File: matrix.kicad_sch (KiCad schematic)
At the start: 129 parts

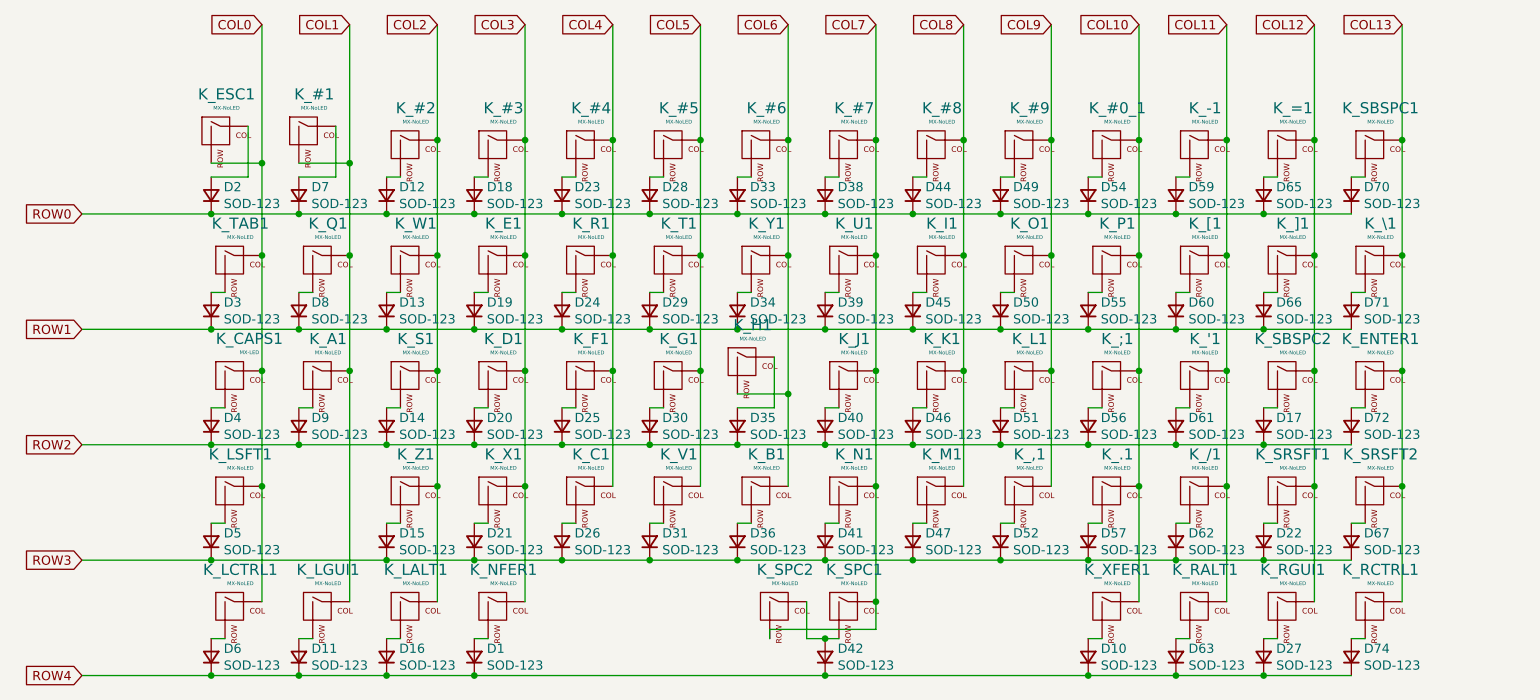
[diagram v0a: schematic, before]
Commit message: Edit Key Matrix
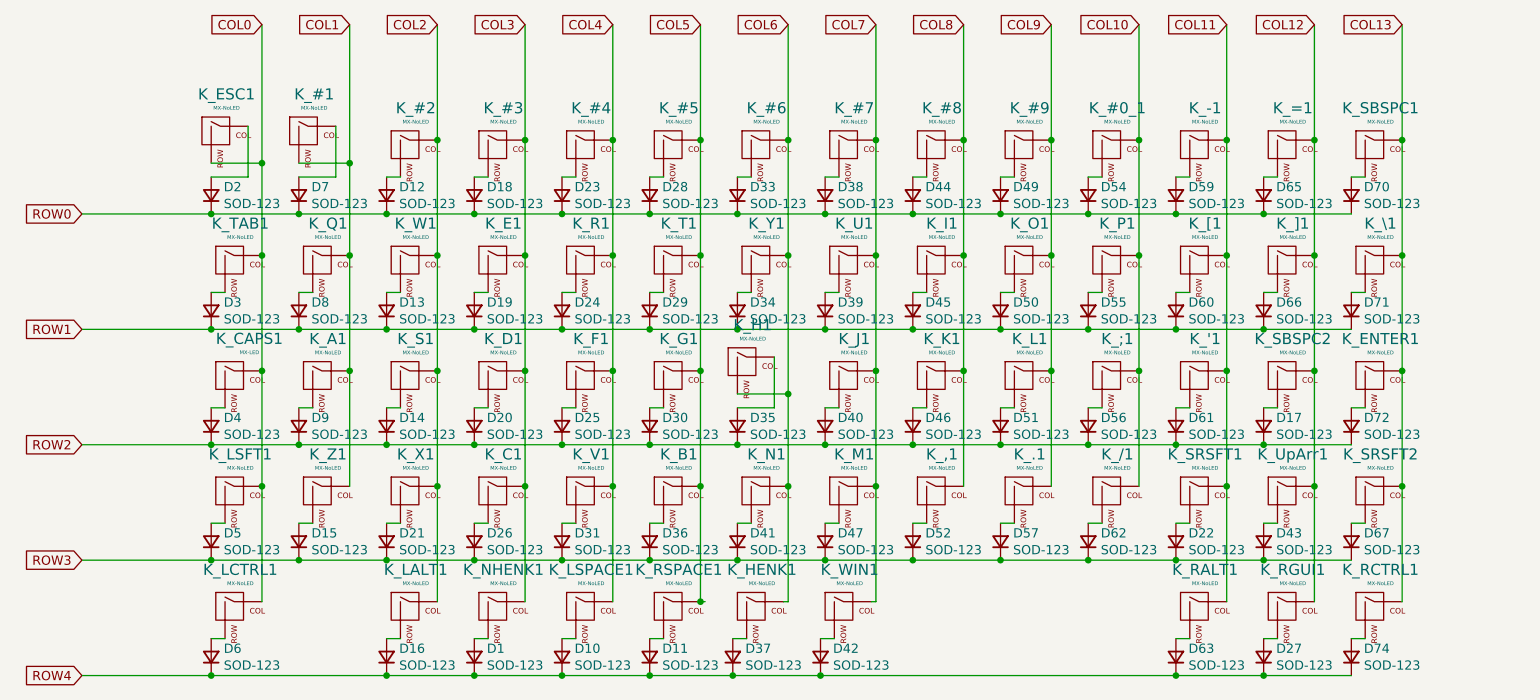
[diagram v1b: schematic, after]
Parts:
- removed K_LGUI1, K_SPC2: MX-NoLED, MX_Only:MXOnly-1U-Hotswap, symbol MX_Alps_Hybrid:MX-NoLED
- removed K_SPC1: MX-NoLED, MX_Only:MXOnly-6U-Centered-Hotswap-ReversedStabilizers, symbol MX_Alps_Hybrid:MX-NoLED
- removed K_XFER1: MX-NoLED, MX_Only:MXOnly-1.25U-Hotswap, symbol MX_Alps_Hybrid:MX-NoLED
- added D37, D43: SOD-123, Diode_SMD:D_SOD-123, symbol Device:D_Small
- added K_HENK1, K_UpArr1, K_WIN1: MX-NoLED, MX_Only:MXOnly-1U-Hotswap, symbol MX_Alps_Hybrid:MX-NoLED
- added K_LSPACE1, K_RSPACE1: MX-NoLED, MX_Only:MXOnly-1.25U-Hotswap, symbol MX_Alps_Hybrid:MX-NoLED
- renumbered K_NFER1 to K_NHENK1
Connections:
- net COL1: now also K_Z1.1 (COL)
- net COL10: now also K_/1.1 (COL); no longer K_.1.1 (COL)
- net COL11: now also K_SRSFT1.1 (COL); no longer K_/1.1 (COL)
- net COL12: now also K_UpArr1.1 (COL); no longer K_SRSFT1.1 (COL)
- net COL2: now also K_X1.1 (COL); no longer K_Z1.1 (COL)
- net COL3: now also K_C1.1 (COL); no longer K_X1.1 (COL)
- net COL4: now also K_V1.1 (COL), K_LSPACE1.1 (COL); no longer K_C1.1 (COL)
- net COL5: now also K_B1.1 (COL), K_RSPACE1.1 (COL); no longer K_V1.1 (COL)
- net COL6: now also K_N1.1 (COL), K_HENK1.1 (COL); no longer K_B1.1 (COL)
- net COL7: now also K_M1.1 (COL), K_WIN1.1 (COL); no longer K_N1.1 (COL)
- net COL8: now also K_,1.1 (COL); no longer K_M1.1 (COL)
- net COL9: now also K_.1.1 (COL); no longer K_,1.1 (COL)
- net ROW3: now also D43.1 (K)
- net ROW4: now also D37.1 (K)
- net at D42.2 (A): now also K_WIN1.2 (ROW)
- net at D11.2 (A): now also K_RSPACE1.2 (ROW)
- net at D10.2 (A): now also K_LSPACE1.2 (ROW)
- new net: D43.2 (A), K_UpArr1.2 (ROW)
- new net: D37.2 (A), K_HENK1.2 (ROW)
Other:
- moved on the sheet: D15, D21, D22, D26, D31, D36, D41, D47, D52, D57, D62, K_,1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

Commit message: edit footprint of Keyswitches.
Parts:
- K_LCTRL1, K_NHENK1: footprint MX_Only:MXOnly-1.25U-Hotswap -> MX_Only:MXOnly-1U-Hotswap
- K_LSFT1: footprint MX_Only:MXOnly-2.25U-Hotswap -> MX_Only:MXOnly-2U-Hotswap
- K_SRSFT2: footprint MX_Only:MXOnly-1.75U-Hotswap -> MX_Only:MXOnly-1U-Hotswap
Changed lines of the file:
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@@
       (effects (font (size 0.508 0.508)))
     )
-    (property "Footprint" "MX_Only:MXOnly-2.25U-Hotswap" (id 2) (at 60.325 102.235 0)
+    (property "Footprint" "MX_Only:MXOnly-2U-Hotswap" (id 2) (at 60.325 102.235 0)
       (effects (font (size 1.524 1.524)) hide)
     )
@@
       (effects (font (size 0.508 0.508)))
     )
-    (property "Footprint" "MX_Only:MXOnly-1.75U-Hotswap" (id 2) (at 217.17 102.235 0)
+    (property "Footprint" "MX_Only:MXOnly-1U-Hotswap" (id 2) (at 217.17 102.235 0)
       (effects (font (size 1.524 1.524)) hide)
     )
@@
       (effects (font (size 0.508 0.508)))
     )
-    (property "Footprint" "MX_Only:MXOnly-1.25U-Hotswap" (id 2) (at 60.325 118.11 0)
+    (property "Footprint" "MX_Only:MXOnly-1U-Hotswap" (id 2) (at 60.325 118.11 0)
       (effects (font (size 1.524 1.524)) hide)
     )
@@
       (effects (font (size 0.508 0.508)))
     )
-    (property "Footprint" "MX_Only:MXOnly-1.25U-Hotswap" (id 2) (at 96.52 118.11 0)
-      (effects (font (size 1.524 1.524)) hide)
-    )
+    (property "Footprint" "MX_Only:MXOnly-1U-Hotswap" (id 2) (at 96.52 118.11 0)
+      (effects (font (size 1.524 1.524)) hide)
+    )

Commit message: Modify Symbol Name
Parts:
- renumbered K_RGUI1 to K_DOWN1, K_RALT1 to K_LEFT1, K_\1 to K_PIPE1, K_RCTRL1 to K_RIGHT1, K_SRSFT2 to K_RSFT1, K_SRSFT1 to K_UNSC1, K_UpArr1 to K_UP1
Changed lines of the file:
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@@
   (symbol (lib_id "MX_Alps_Hybrid:MX-NoLED") (at 233.045 69.85 0) (unit 1)
     (in_bom yes) (on_board yes)
-    (property "Reference" "K_\\1" (id 0) (at 233.8832 64.1858 0)
+    (property "Reference" "K_PIPE1" (id 0) (at 233.8832 64.1858 0)
       (effects (font (size 1.524 1.524)))
     )
@@
   (symbol (lib_id "MX_Alps_Hybrid:MX-NoLED") (at 233.045 101.6 0) (unit 1)
     (in_bom yes) (on_board yes)
-    (property "Reference" "K_SRSFT2" (id 0) (at 233.8832 95.9358 0)
+    (property "Reference" "K_RSFT1" (id 0) (at 233.8832 95.9358 0)
       (effects (font (size 1.524 1.524)))
     )
@@
   (symbol (lib_id "MX_Alps_Hybrid:MX-NoLED") (at 208.915 117.475 0) (unit 1)
     (in_bom yes) (on_board yes)
-    (property "Reference" "K_RALT1" (id 0) (at 209.7532 111.8108 0)
+    (property "Reference" "K_LEFT1" (id 0) (at 209.7532 111.8108 0)
       (effects (font (size 1.524 1.524)))
     )
@@
   (symbol (lib_id "MX_Alps_Hybrid:MX-NoLED") (at 233.045 117.475 0) (unit 1)
     (in_bom yes) (on_board yes)
-    (property "Reference" "K_RCTRL1" (id 0) (at 233.8832 111.8108 0)
+    (property "Reference" "K_RIGHT1" (id 0) (at 233.8832 111.8108 0)
       (effects (font (size 1.524 1.524)))
     )
@@
   (symbol (lib_id "MX_Alps_Hybrid:MX-NoLED") (at 208.915 101.6 0) (unit 1)
     (in_bom yes) (on_board yes)
-    (property "Reference" "K_SRSFT1" (id 0) (at 209.7532 95.9358 0)
+    (property "Reference" "K_UNSC1" (id 0) (at 209.7532 95.9358 0)
       (effects (font (size 1.524 1.524)))
     )
@@
   (symbol (lib_id "MX_Alps_Hybrid:MX-NoLED") (at 220.98 117.475 0) (unit 1)
     (in_bom yes) (on_board yes)
-    (property "Reference" "K_RGUI1" (id 0) (at 221.8182 111.8108 0)
+    (property "Reference" "K_DOWN1" (id 0) (at 221.8182 111.8108 0)
       (effects (font (size 1.524 1.524)))
     )
@@
   (symbol (lib_id "MX_Alps_Hybrid:MX-NoLED") (at 220.98 101.6 0) (unit 1)
     (in_bom yes) (on_board yes)
-    (property "Reference" "K_UpArr1" (id 0) (at 221.8182 95.9358 0)
-      (effects (font (size 1.524 1.524)))
-    )
+    (property "Reference" "K_UP1" (id 0) (at 221.8182 95.9358 0)
+      (effects (font (size 1.524 1.524)))
+    )

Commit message: Diodeの配置完了
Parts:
- renumbered K_'1 to K_:1, K_[1 to K_@1, K_SBSPC2 to K_BKSPC1, K_SBSPC1 to K_PIPE1, K_]1 to K_[1, K_PIPE1 to K_]2
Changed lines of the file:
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@@
   (symbol (lib_id "MX_Alps_Hybrid:MX-NoLED") (at 233.045 53.975 0) (unit 1)
     (in_bom yes) (on_board yes)
-    (property "Reference" "K_SBSPC1" (id 0) (at 233.8832 48.3108 0)
+    (property "Reference" "K_PIPE1" (id 0) (at 233.8832 48.3108 0)
       (effects (font (size 1.524 1.524)))
     )
@@
   (symbol (lib_id "MX_Alps_Hybrid:MX-NoLED") (at 208.915 69.85 0) (unit 1)
     (in_bom yes) (on_board yes)
-    (property "Reference" "K_[1" (id 0) (at 209.7532 64.1858 0)
+    (property "Reference" "K_@1" (id 0) (at 209.7532 64.1858 0)
       (effects (font (size 1.524 1.524)))
     )
@@
   (symbol (lib_id "MX_Alps_Hybrid:MX-NoLED") (at 220.98 69.85 0) (unit 1)
     (in_bom yes) (on_board yes)
-    (property "Reference" "K_]1" (id 0) (at 221.8182 64.1858 0)
+    (property "Reference" "K_[1" (id 0) (at 221.8182 64.1858 0)
       (effects (font (size 1.524 1.524)))
     )
@@
   (symbol (lib_id "MX_Alps_Hybrid:MX-NoLED") (at 233.045 69.85 0) (unit 1)
     (in_bom yes) (on_board yes)
-    (property "Reference" "K_PIPE1" (id 0) (at 233.8832 64.1858 0)
+    (property "Reference" "K_]2" (id 0) (at 233.8832 64.1858 0)
       (effects (font (size 1.524 1.524)))
     )
@@
   (symbol (lib_id "MX_Alps_Hybrid:MX-NoLED") (at 208.915 85.725 0) (unit 1)
     (in_bom yes) (on_board yes)
-    (property "Reference" "K_'1" (id 0) (at 209.7532 80.0608 0)
+    (property "Reference" "K_:1" (id 0) (at 209.7532 80.0608 0)
       (effects (font (size 1.524 1.524)))
     )
@@
   (symbol (lib_id "MX_Alps_Hybrid:MX-NoLED") (at 220.98 85.725 0) (unit 1)
     (in_bom yes) (on_board yes)
-    (property "Reference" "K_SBSPC2" (id 0) (at 221.8182 80.0608 0)
-      (effects (font (size 1.524 1.524)))
-    )
+    (property "Reference" "K_BKSPC1" (id 0) (at 221.8182 80.0608 0)
+      (effects (font (size 1.524 1.524)))
+    )

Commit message: 時間的にいったんここまで
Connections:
- net COL6: now also K_H1.1 (COL); no longer K_H1.2 (ROW)
- net at D35.2 (A): now also K_H1.2 (ROW); no longer K_H1.1 (COL)
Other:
- moved on the sheet: K_H1
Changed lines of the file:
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@@
   (junction (at 181.61 110.49) (diameter 0) (color 0 0 0 0)
   )
+  (junction (at 152.4 84.455) (diameter 0) (color 0 0 0 0)
+  )
   (junction (at 109.22 78.74) (diameter 0) (color 0 0 0 0)
   )
@@
   (junction (at 73.025 62.865) (diameter 0) (color 0 0 0 0)
   )
-  (junction (at 152.4 87.63) (diameter 0) (color 0 0 0 0)
-  )
   (junction (at 188.595 52.705) (diameter 0) (color 0 0 0 0)
   )
@@
     (stroke (width 0) (type default) (color 0 0 0 0))
   )
-  (wire (pts (xy 145.415 89.535) (xy 150.495 89.535))
-    (stroke (width 0) (type default) (color 0 0 0 0))
-  )
   (wire (pts (xy 193.675 110.49) (xy 181.61 110.49))
     (stroke (width 0) (type default) (color 0 0 0 0))
@@
     (stroke (width 0) (type default) (color 0 0 0 0))
   )
-  (wire (pts (xy 145.415 87.63) (xy 152.4 87.63))
-    (stroke (width 0) (type default) (color 0 0 0 0))
-  )
   (wire (pts (xy 229.87 94.615) (xy 217.805 94.615))
     (stroke (width 0) (type default) (color 0 0 0 0))
@@
     (stroke (width 0) (type default) (color 0 0 0 0))
   )
+  (wire (pts (xy 145.415 89.535) (xy 147.32 89.535))
+    (stroke (width 0) (type default) (color 0 0 0 0))
+  )
   (wire (pts (xy 181.61 62.865) (xy 193.675 62.865))
     (stroke (width 0) (type default) (color 0 0 0 0))
@@
     (stroke (width 0) (type default) (color 0 0 0 0))
   )
+  (wire (pts (xy 152.4 84.455) (xy 152.4 100.33))
+    (stroke (width 0) (type default) (color 0 0 0 0))
+  )
   (wire (pts (xy 73.025 94.615) (xy 55.245 94.615))
     (stroke (width 0) (type default) (color 0 0 0 0))
@@
     (stroke (width 0) (type default) (color 0 0 0 0))
   )
-  (wire (pts (xy 152.4 68.58) (xy 152.4 87.63))
+  (wire (pts (xy 152.4 68.58) (xy 152.4 84.455))
     (stroke (width 0) (type default) (color 0 0 0 0))
   )
@@
     (stroke (width 0) (type default) (color 0 0 0 0))
   )
-  (wire (pts (xy 150.495 82.55) (xy 150.495 89.535))
-    (stroke (width 0) (type default) (color 0 0 0 0))
-  )
   (wire (pts (xy 73.025 121.285) (xy 74.93 121.285))
     (stroke (width 0) (type default) (color 0 0 0 0))
@@
   )
   (wire (pts (xy 85.09 62.865) (xy 97.155 62.865))
-    (stroke (width 0) (type default) (color 0 0 0 0))
-  )
-  (wire (pts (xy 152.4 87.63) (xy 152.4 100.33))
     (stroke (width 0) (type default) (color 0 0 0 0))
   )
@@
     (pin "2")
   )
-  (symbol (lib_id "MX_Alps_Hybrid:MX-NoLED") (at 146.685 83.82 0) (unit 1)
-    (in_bom yes) (on_board yes)
-    (property "Reference" "K_H1" (id 0) (at 147.5232 78.1558 0)
-      (effects (font (size 1.524 1.524)))
-    )
-    (property "Value" "MX-NoLED" (id 1) (at 147.5232 80.0354 0)
-      (effects (font (size 0.508 0.508)))
-    )
-    (property "Footprint" "MX_Only:MXOnly-1U-Hotswap" (id 2) (at 130.81 84.455 0)
-      (effects (font (size 1.524 1.524)) hide)
-    )
-    (property "Datasheet" "" (id 3) (at 130.81 84.455 0)
-      (effects (font (size 1.524 1.524)) hide)
-    )
+  (symbol (lib_id "MX_Alps_Hybrid:MX-NoLED") (at 148.59 85.725 0) (unit 1)
+    (in_bom yes) (on_board yes)
+    (property "Reference" "K_H1" (id 0) (at 149.4282 80.0608 0)
+      (effects (font (size 1.524 1.524)))
+    )
+    (property "Value" "MX-NoLED" (id 1) (at 149.4282 81.9404 0)
+      (effects (font (size 0.508 0.508)))
+    )
+    (property "Footprint" "MX_Only:MXOnly-1U-Hotswap" (id 2) (at 132.715 86.36 0)
+      (effects (font (size 1.524 1.524)) hide)
+    )
+    (property "Datasheet" "" (id 3) (at 132.715 86.36 0)
+      (effects (font (size 1.524 1.524)) hide)
+    )

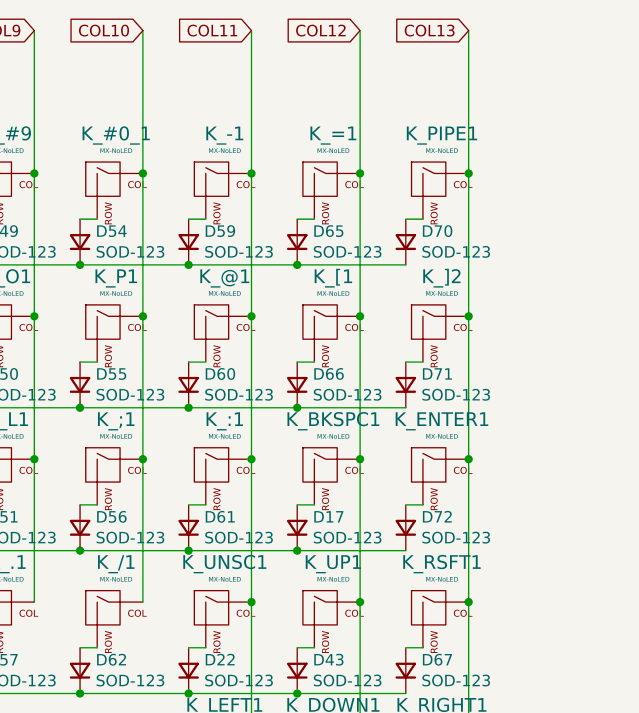
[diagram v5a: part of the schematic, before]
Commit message: 回路図エディターで COL14を追加
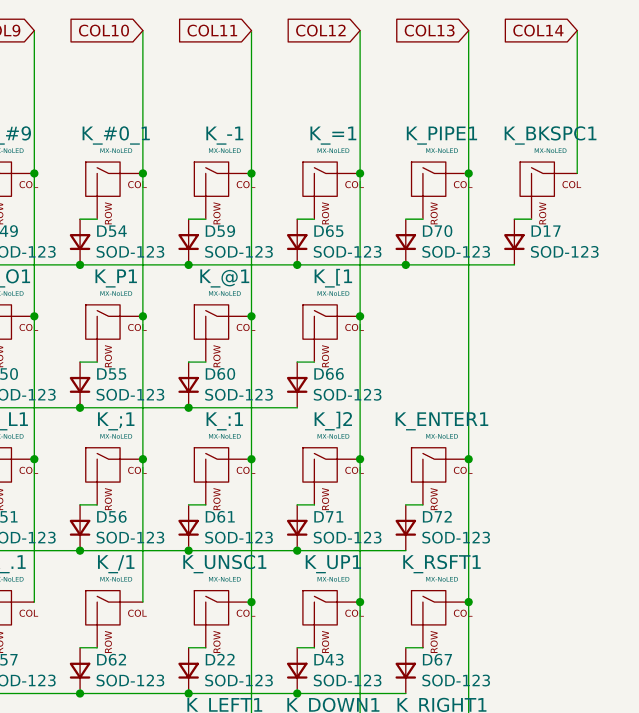
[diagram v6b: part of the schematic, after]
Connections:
- net COL12: now also K_]2.1 (COL); no longer K_BKSPC1.1 (COL)
- net COL13: no longer K_]2.1 (COL)
- net ROW0: now also D17.1 (K)
- net ROW1: no longer D71.1 (K)
- net ROW2: now also D71.1 (K); no longer D17.1 (K)
- new net COL14: K_BKSPC1.1 (COL)
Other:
- moved on the sheet: D17, D71, K_BKSPC1, K_]2
